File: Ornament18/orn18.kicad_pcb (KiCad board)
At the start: 2 copper layers, 50 x 50 mm, 13 parts, among them SW1 SW_Push, U1 ATTINY13A-SSU, U2 74LS138

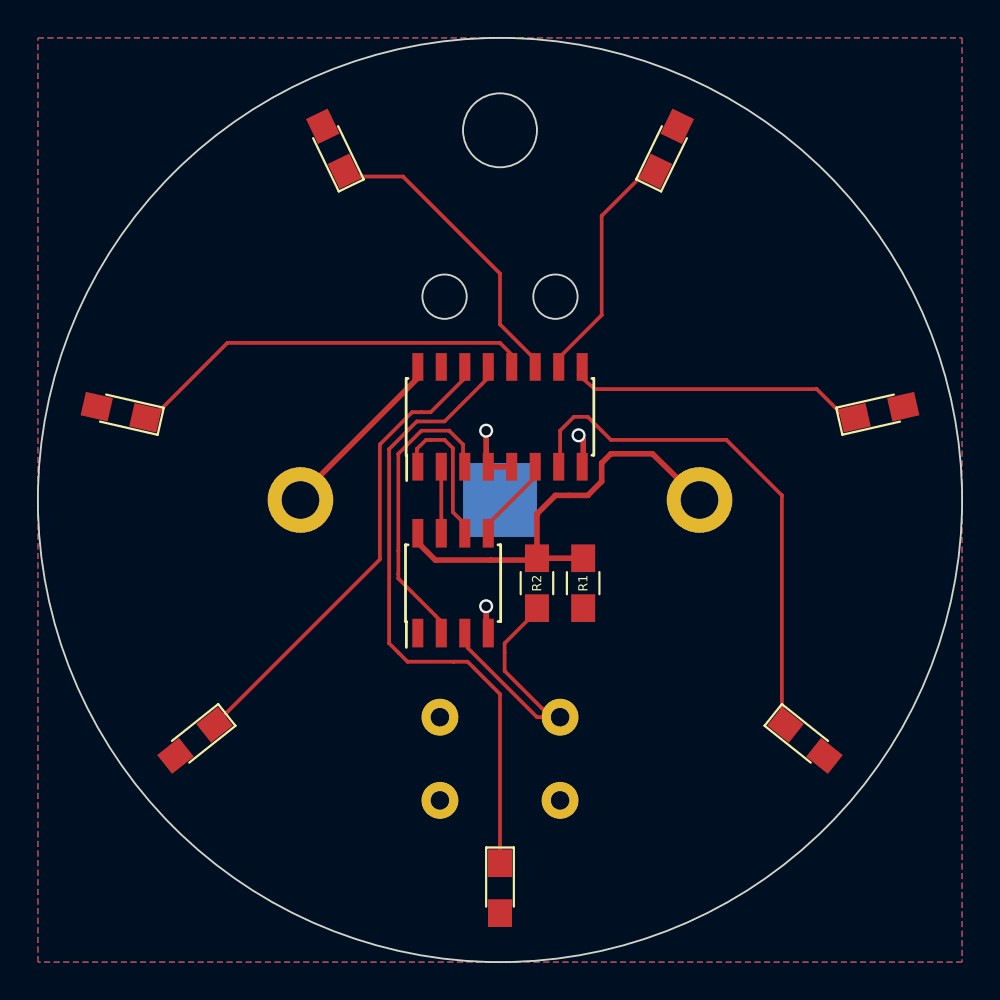
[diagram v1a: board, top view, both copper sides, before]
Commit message: fix mechanical holes; add placeholder for allpcb id
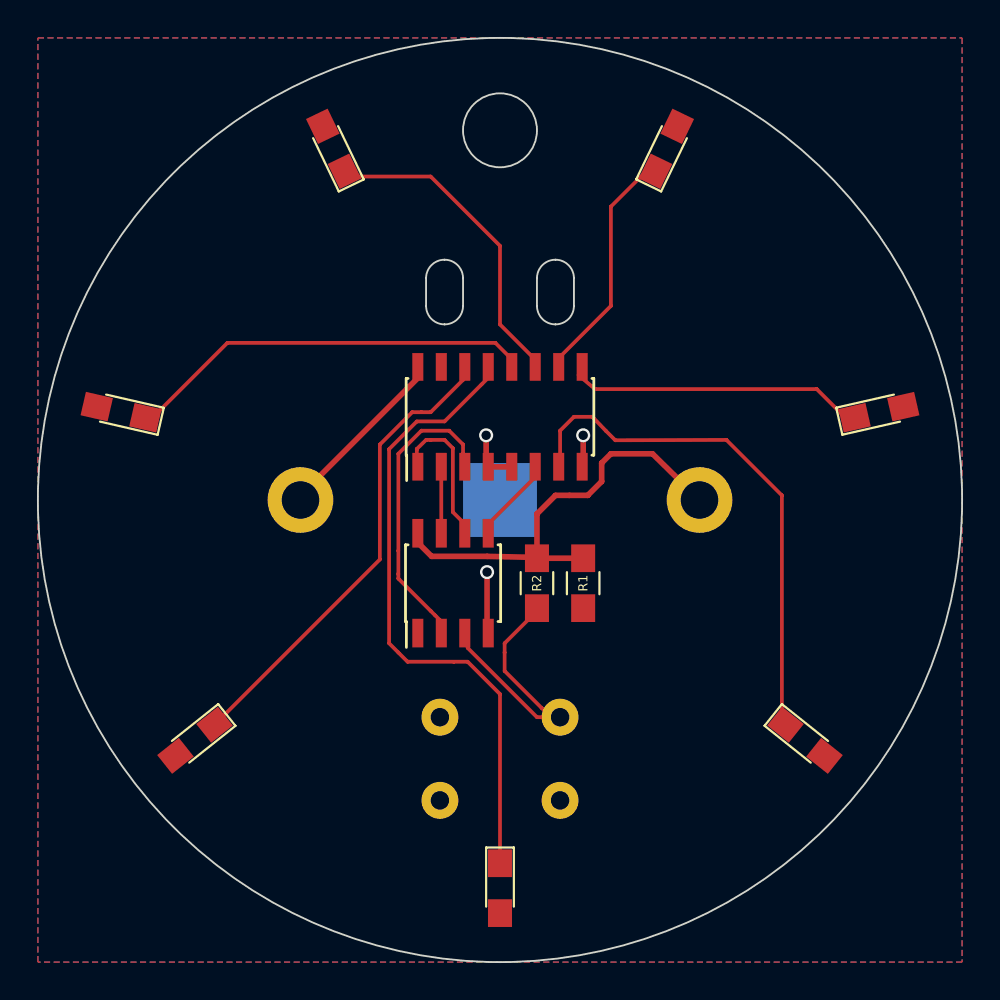
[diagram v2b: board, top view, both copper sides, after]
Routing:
- net GND: track 6.59 -> 8.11 mm
- net Net-(D4-Pad1): track 16.7 -> 17.6 mm
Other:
- outline, holes or cut-outs redrawn
- board text added: "ALL-"
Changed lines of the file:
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@@
     (area 114.949999 74.949999 165.050001 125.050001)
     (thickness 1.6)
-    (drawings 4)
-    (tracks 130)
+    (drawings 20)
+    (tracks 129)
     (zones 0)
     (modules 13)
@@
     (mod_text_size 1 1)
     (mod_text_width 0.15)
-    (pad_size 1.5 1.5)
-    (pad_drill 0.6)
+    (pad_size 1.5 1.3)
+    (pad_drill 0)
     (pad_to_mask_clearance 0)
     (aux_axis_origin 0 0)
@@
     )
   )
-  (gr_circle (center 137 89) (end 137 90.2) (layer Edge.Cuts) (width 0.1))
-  (gr_circle (center 143 89) (end 143 90.2) (layer Edge.Cuts) (width 0.1))
+  (gr_text "ALL-          " (at 140 106) (layer B.SilkS)
+    (effects (font (size 1.2 1.2) (thickness 0.1)) (justify mirror))
+  )
+  (gr_line (start 132.5 104.5) (end 132.5 107.25) (angle 90) (layer B.SilkS) (width 0.1))
+  (gr_line (start 147.5 104.5) (end 132.5 104.5) (angle 90) (layer B.SilkS) (width 0.1))
+  (gr_line (start 147.5 107.25) (end 147.5 104.5) (angle 90) (layer B.SilkS) (width 0.1))
+  (gr_line (start 132.5 107.25) (end 147.5 107.25) (angle 90) (layer B.SilkS) (width 0.1))
+  (gr_circle (center 140 100) (end 140 110) (layer B.CrtYd) (width 0.2))
+  (gr_line (start 136 88) (end 136 89.5) (angle 90) (layer Edge.Cuts) (width 0.1))
+  (gr_line (start 138 88) (end 138 89.5) (angle 90) (layer Edge.Cuts) (width 0.1))
+  (gr_line (start 144 88) (end 144 89.5) (angle 90) (layer Edge.Cuts) (width 0.1))
+  (gr_line (start 142 88) (end 142 89.5) (angle 90) (layer Edge.Cuts) (width 0.1))
+  (gr_arc (start 137 88) (end 136 88) (angle 90) (layer Edge.Cuts) (width 0.1))
+  (gr_arc (start 137 88) (end 137 87) (angle 90) (layer Edge.Cuts) (width 0.1))
+  (gr_arc (start 143 88) (end 142 88) (angle 90) (layer Edge.Cuts) (width 0.1))
+  (gr_arc (start 143 88) (end 143 87) (angle 90) (layer Edge.Cuts) (width 0.1))
+  (gr_arc (start 137 89.5) (end 138 89.5) (angle 90) (layer Edge.Cuts) (width 0.1))
+  (gr_arc (start 137 89.5) (end 137 90.5) (angle 90) (layer Edge.Cuts) (width 0.1))
+  (gr_arc (start 143 89.5) (end 144 89.5) (angle 90) (layer Edge.Cuts) (width 0.1))
+  (gr_arc (start 143 89.5) (end 143 90.5) (angle 90) (layer Edge.Cuts) (width 0.1))
   (gr_circle (center 140 80) (end 140 82) (layer Edge.Cuts) (width 0.1))
   (gr_circle (center 140 100) (end 140 125) (layer Edge.Cuts) (width 0.1))
   (segment (start 144.445 98.2) (end 144.5 98.145) (width 0.3048) (layer F.Cu) (net 1))
-  (segment (start 144.5 98.145) (end 144.5 96.75) (width 0.3048) (layer F.Cu) (net 1))
-  (segment (start 144.5 96.75) (end 144.25 96.5) (width 0.3048) (layer F.Cu) (net 1))
-  (via (at 144.25 96.5) (size 0.762) (drill 0.508) (layers F.Cu B.Cu) (net 1))
+  (segment (start 144.5 98.145) (end 144.5 96.5) (width 0.3048) (layer F.Cu) (net 1))
+  (via (at 144.5 96.5) (size 0.762) (drill 0.508) (layers F.Cu B.Cu) (net 1))
   (segment (start 139.365 98.2) (end 139.25 98.085) (width 0.3048) (layer F.Cu) (net 1))
-  (segment (start 139.25 98.085) (end 139.25 96.25) (width 0.3048) (layer F.Cu) (net 1))
-  (via (at 139.25 96.25) (size 0.762) (drill 0.508) (layers F.Cu B.Cu) (net 1))
-  (segment (start 139.365 107.2) (end 139.25 107.085) (width 0.3048) (layer F.Cu) (net 1))
-  (segment (start 139.25 107.085) (end 139.25 105.75) (width 0.3048) (layer F.Cu) (net 1))
-  (via (at 139.25 105.75) (size 0.762) (drill 0.508) (layers F.Cu B.Cu) (net 1))
+  (segment (start 139.25 98.085) (end 139.25 96.5) (width 0.3048) (layer F.Cu) (net 1))
+  (via (at 139.25 96.5) (size 0.762) (drill 0.508) (layers F.Cu B.Cu) (net 1))
+  (segment (start 139.365 107.2) (end 139.3 107.2) (width 0.3048) (layer F.Cu) (net 1))
+  (segment (start 139.3 107.2) (end 139.3 103.9) (width 0.3048) (layer F.Cu) (net 1))
+  (via (at 139.3 103.9) (size 0.762) (drill 0.508) (layers F.Cu B.Cu) (net 1))
   (segment (start 139.365 98.2) (end 140.635 98.2) (width 0.3048) (layer F.Cu) (net 1))
   (segment (start 135.555 101.8) (end 135.5 101.855) (width 0.3048) (layer F.Cu) (net 2))
   (segment (start 135.5 101.855) (end 135.5 102.25) (width 0.3048) (layer F.Cu) (net 2))
-  (segment (start 141.75 103.25) (end 142 103.15) (width 0.3048) (layer F.Cu) (net 2))
-  (segment (start 139.5 103.25) (end 141.75 103.25) (width 0.3048) (layer F.Cu) (net 2))
-  (segment (start 136.5 103.25) (end 139.5 103.25) (width 0.3048) (layer F.Cu) (net 2))
-  (segment (start 135.5 102.25) (end 136.5 103.25) (width 0.3048) (layer F.Cu) (net 2))
+  (segment (start 141.7 103.1) (end 142 103.15) (width 0.3048) (layer F.Cu) (net 2))
+  (segment (start 139.3 103.05) (end 141.7 103.1) (width 0.3048) (layer F.Cu) (net 2))
+  (segment (start 136.3 103.05) (end 139.3 103.05) (width 0.3048) (layer F.Cu) (net 2))
+  (segment (start 135.5 102.25) (end 136.3 103.05) (width 0.3048) (layer F.Cu) (net 2))
   (segment (start 129.205 99.75) (end 135.555 93.4) (width 0.3048) (layer F.Cu) (net 2))
   (segment (start 135.555 93.4) (end 135.555 92.8) (width 0.3048) (layer F.Cu) (net 2))
@@
   (segment (start 139.365 92.8) (end 139.5 93) (width 0.2032) (layer F.Cu) (net 5))
   (segment (start 140.635 92.8) (end 140.75 92.685) (width 0.2032) (layer F.Cu) (net 6))
-  (segment (start 140.75 92.685) (end 140.75 92.25) (width 0.2032) (layer F.Cu) (net 6))
-  (segment (start 140.75 92.25) (end 140 91.5) (width 0.2032) (layer F.Cu) (net 6))
-  (segment (start 140 91.5) (end 125.25 91.5) (width 0.2032) (layer F.Cu) (net 6))
+  (segment (start 140.75 92.685) (end 140.5 92.25) (width 0.2032) (layer F.Cu) (net 6))
+  (segment (start 140.5 92.25) (end 139.75 91.5) (width 0.2032) (layer F.Cu) (net 6))
+  (segment (start 139.75 91.5) (end 125.25 91.5) (width 0.2032) (layer F.Cu) (net 6))
   (segment (start 125.25 91.5) (end 121.25 95.5) (width 0.2032) (layer F.Cu) (net 6))
   (segment (start 131.58544 82.216454) (end 131.868986 82.5) (width 0.2032) (layer F.Cu) (net 7))
   (segment (start 141.75 92.25) (end 141.75 92.645) (width 0.2032) (layer F.Cu) (net 7))
   (segment (start 140 90.5) (end 141.75 92.25) (width 0.2032) (layer F.Cu) (net 7))
-  (segment (start 140 87.75) (end 140 90.5) (width 0.2032) (layer F.Cu) (net 7))
-  (segment (start 134.75 82.5) (end 140 87.75) (width 0.2032) (layer F.Cu) (net 7))
-  (segment (start 131.868986 82.5) (end 134.75 82.5) (width 0.2032) (layer F.Cu) (net 7))
+  (segment (start 140 86.25) (end 140 90.5) (width 0.2032) (layer F.Cu) (net 7))
+  (segment (start 136.25 82.5) (end 140 86.25) (width 0.2032) (layer F.Cu) (net 7))
+  (segment (start 131.868986 82.5) (end 136.25 82.5) (width 0.2032) (layer F.Cu) (net 7))
   (segment (start 141.75 92.645) (end 141.905 92.8) (width 0.2032) (layer F.Cu) (net 7))
   (segment (start 141.905 92.8) (end 142 92.705) (width 0.2032) (layer F.Cu) (net 7))
   (segment (start 143.175 92.8) (end 143.25 92.725) (width 0.2032) (layer F.Cu) (net 8))
   (segment (start 143.25 92.725) (end 143.25 92.25) (width 0.2032) (layer F.Cu) (net 8))
-  (segment (start 143.25 92.25) (end 145.5 90) (width 0.2032) (layer F.Cu) (net 8))
-  (segment (start 145.5 90) (end 145.5 84.627868) (width 0.2032) (layer F.Cu) (net 8))
-  (segment (start 145.5 84.627868) (end 148.412438 81.71543) (width 0.2032) (layer F.Cu) (net 8))
+  (segment (start 143.25 92.25) (end 146 89.5) (width 0.2032) (layer F.Cu) (net 8))
+  (segment (start 146 89.5) (end 146 84.127868) (width 0.2032) (layer F.Cu) (net 8))
+  (segment (start 146 84.127868) (end 148.412438 81.71543) (width 0.2032) (layer F.Cu) (net 8))
   (segment (start 144.25 93.25) (end 145.145 94) (width 0.2032) (layer F.Cu) (net 9))
   (segment (start 157.134458 94) (end 158.683548 95.54909) (width 0.2032) (layer F.Cu) (net 9))
@@
   (segment (start 143.175 98.2) (end 143.25 98.125) (width 0.2032) (layer F.Cu) (net 10))
   (segment (start 143.25 98.125) (end 143.25 96.25) (width 0.2032) (layer F.Cu) (net 10))
-  (segment (start 146 96.75) (end 152.25 96.75) (width 0.2032) (layer F.Cu) (net 10))
-  (segment (start 145.5 96.25) (end 146 96.75) (width 0.2032) (layer F.Cu) (net 10))
-  (segment (start 144.75 95.5) (end 145.5 96.25) (width 0.2032) (layer F.Cu) (net 10))
-  (segment (start 144.75 95.5) (end 144.75 95.5) (width 0.2032) (layer F.Cu) (net 10))
-  (segment (start 144.75 95.5) (end 144.75 95.5) (width 0.2032) (layer F.Cu) (net 10))
-  (segment (start 144 95.5) (end 144.75 95.5) (width 0.2032) (layer F.Cu) (net 10))
+  (segment (start 146.236538 96.767308) (end 152.25 96.75) (width 0.2032) (layer F.Cu) (net 10))
+  (segment (start 145.736538 96.267308) (end 146.236538 96.767308) (width 0.2032) (layer F.Cu) (net 10))
+  (segment (start 145 95.5) (end 145.736538 96.267308) (width 0.2032) (layer F.Cu) (net 10))
+  (segment (start 145 95.5) (end 145 95.5) (width 0.2032) (layer F.Cu) (net 10))
+  (segment (start 145 95.5) (end 145 95.5) (width 0.2032) (layer F.Cu) (net 10))
+  (segment (start 144 95.5) (end 145 95.5) (width 0.2032) (layer F.Cu) (net 10))
   (segment (start 143.25 96.25) (end 144 95.5) (width 0.2032) (layer F.Cu) (net 10))
   (segment (start 152.25 96.75) (end 155.25 99.75) (width 0.2032) (layer F.Cu) (net 10))

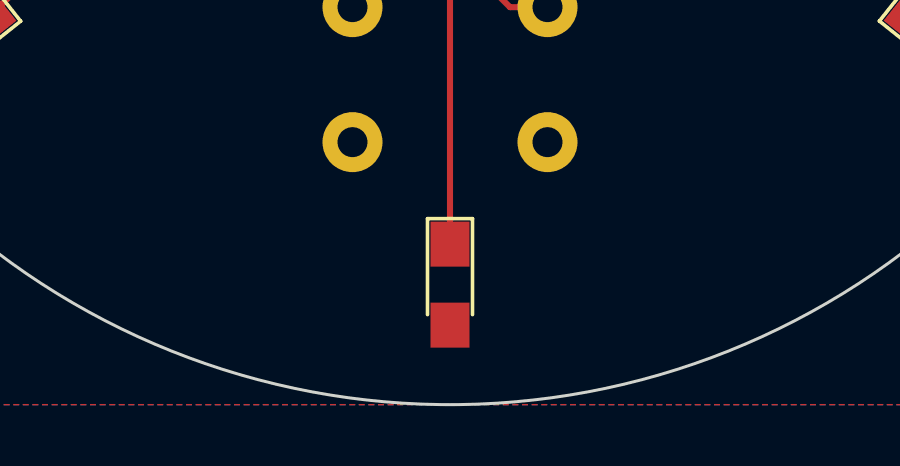
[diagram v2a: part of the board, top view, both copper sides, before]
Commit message: remove silk screen; add signature
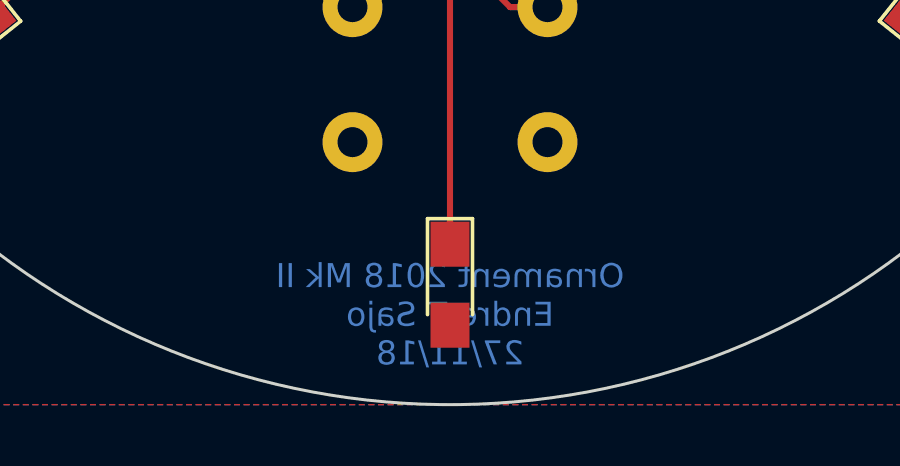
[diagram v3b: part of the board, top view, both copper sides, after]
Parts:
- BT1: footprint orn18:Keystone_3035 -> orn18:Keystone_3035_nosilk
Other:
- board text added: "Ornament 2018 Mk II Endre T Sajo 27/11/18"
- board text removed: "ALL-"

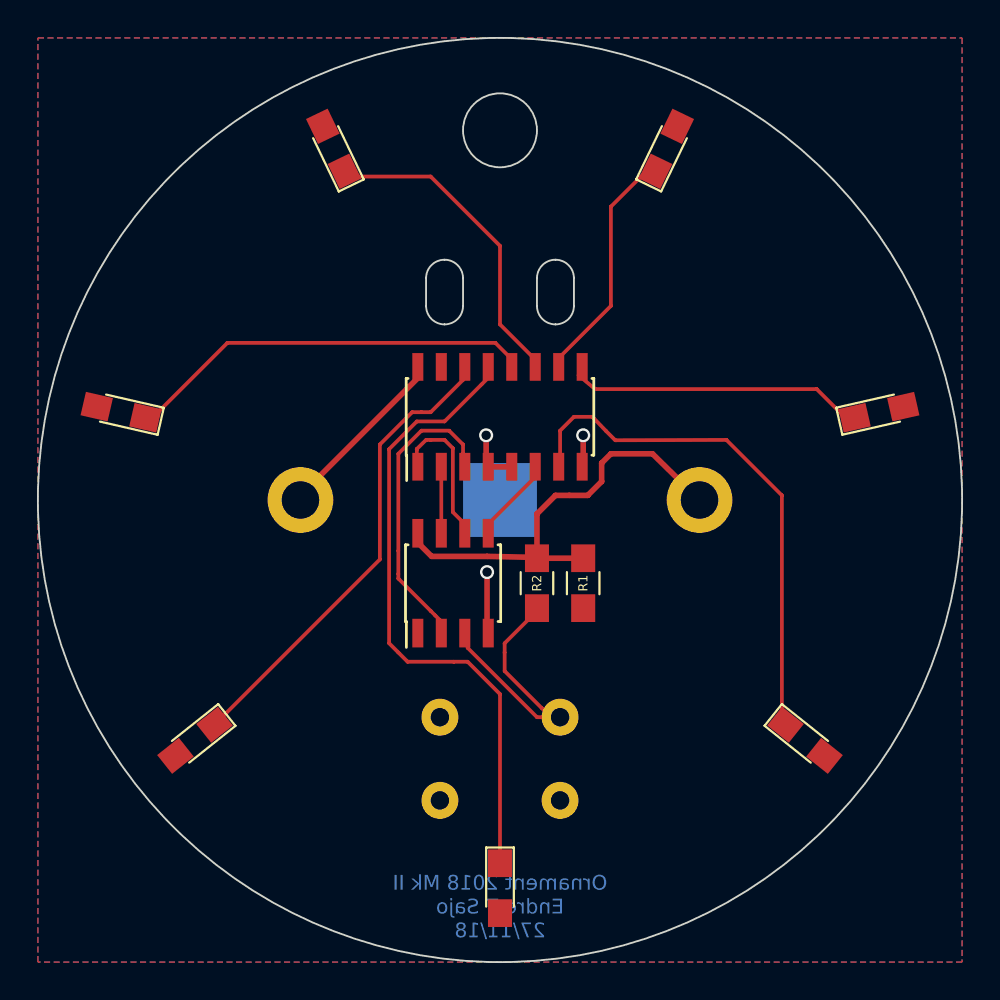
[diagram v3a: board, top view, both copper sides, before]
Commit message: bring ics closer together
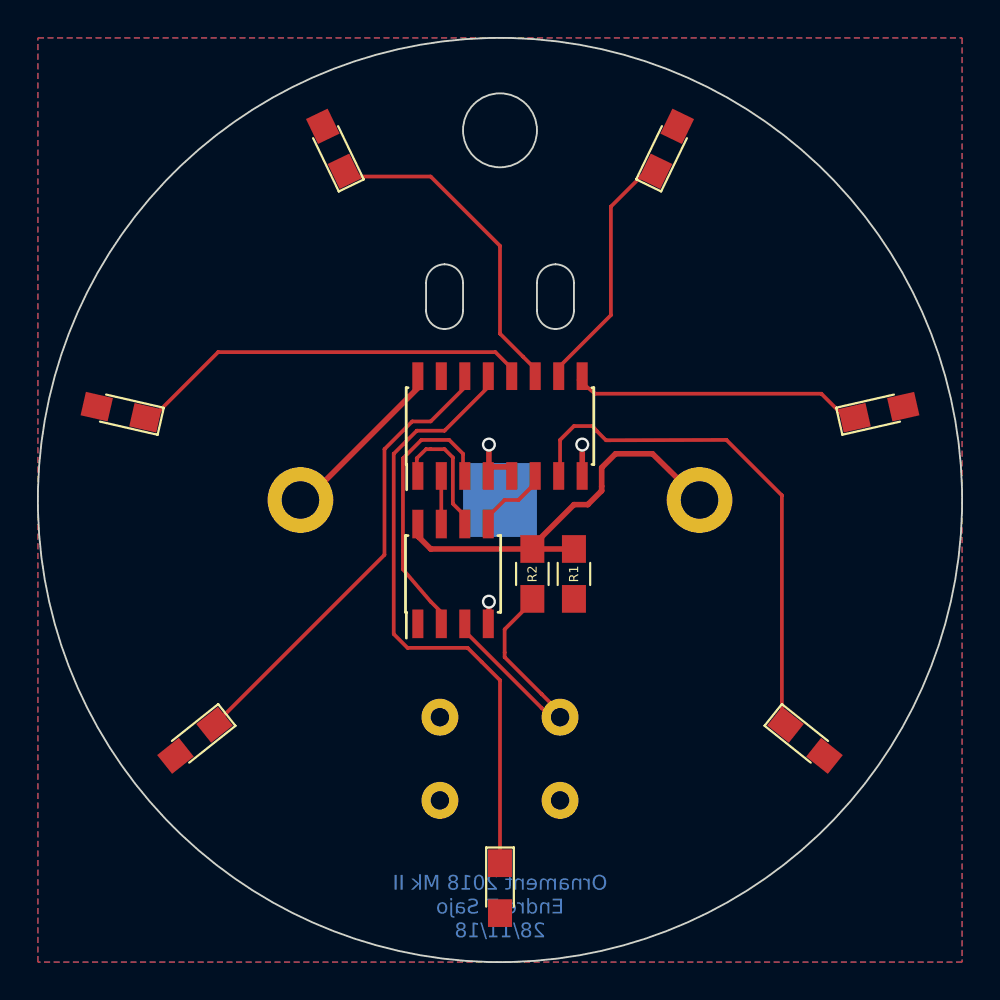
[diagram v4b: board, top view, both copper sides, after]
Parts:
- moved R1 0.71 mm to (144.0, 104.0)
- moved R2 0.56 mm to (141.8, 104.0)
- moved U1 0.50 mm to (137.5, 104.0)
- moved U2 0.50 mm to (140.0, 96.0)
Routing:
- net GND: track 8.11 -> 4.98 mm
- net Net-(U1-Pad2): track 16.3 -> 15.1 mm
- net Net-(U1-Pad6): track 7.47 -> 6.59 mm
- net Net-(D7-Pad1): track 28.6 -> 27.9 mm
- net Net-(R2-Pad2): track 16.0 -> 16.6 mm
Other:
- outline, holes or cut-outs redrawn
- board text added: "Ornament 2018 Mk II Endre T Sajo 28/11/18"
- board text removed: "Ornament 2018 Mk II Endre T Sajo 27/11/18"

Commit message: add silk screen
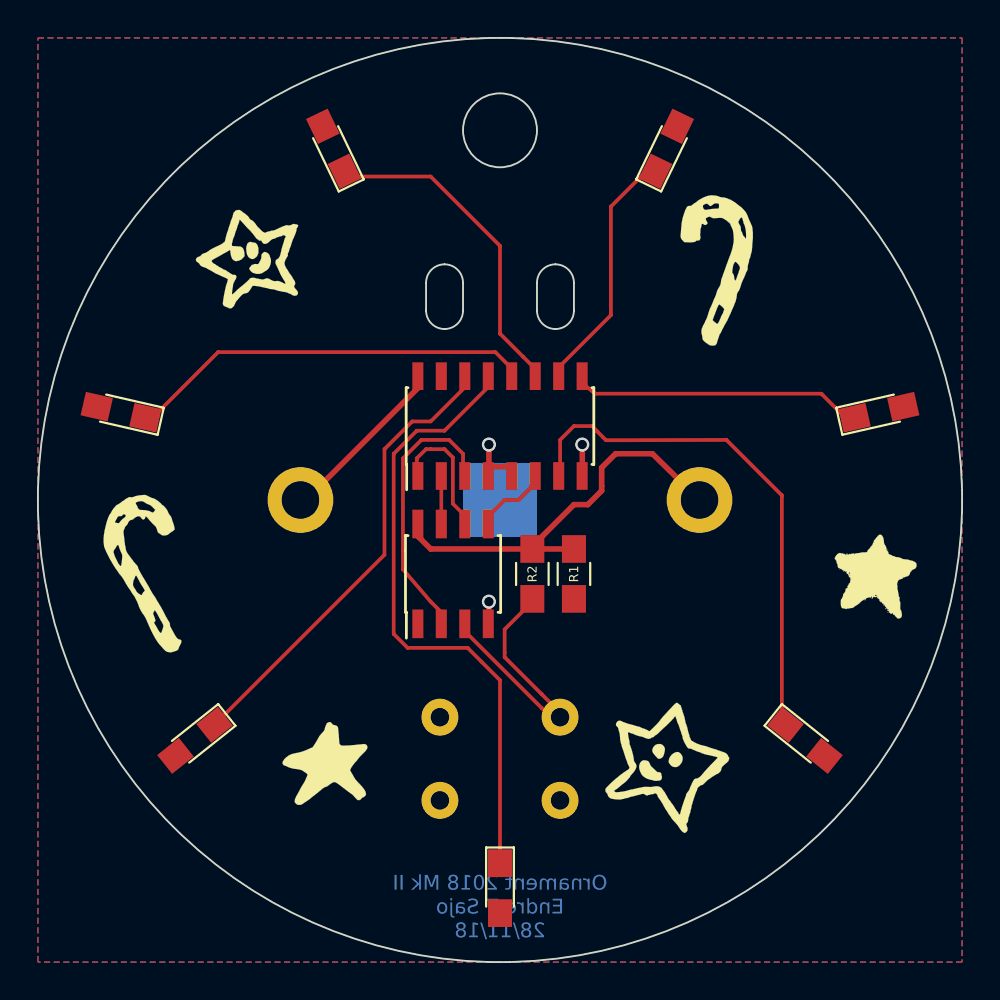
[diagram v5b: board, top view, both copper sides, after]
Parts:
- added G***: LOGO, img:fsilk, F.Cu at (140.0, 100.0)
- added G***: LOGO, img:fsilk, B.Cu at (140.0, 100.0)
